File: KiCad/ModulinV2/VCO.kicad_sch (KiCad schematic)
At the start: 99 parts, among them IC13 AS3340D, IC14 AS3340D, IC15 TL074HIDR, IC16 TL074HIDR, IC17 TL072HIDR, Q1 MMBFJ201, Q2 MMBFJ201, SW1 SW_SPDT_MSM

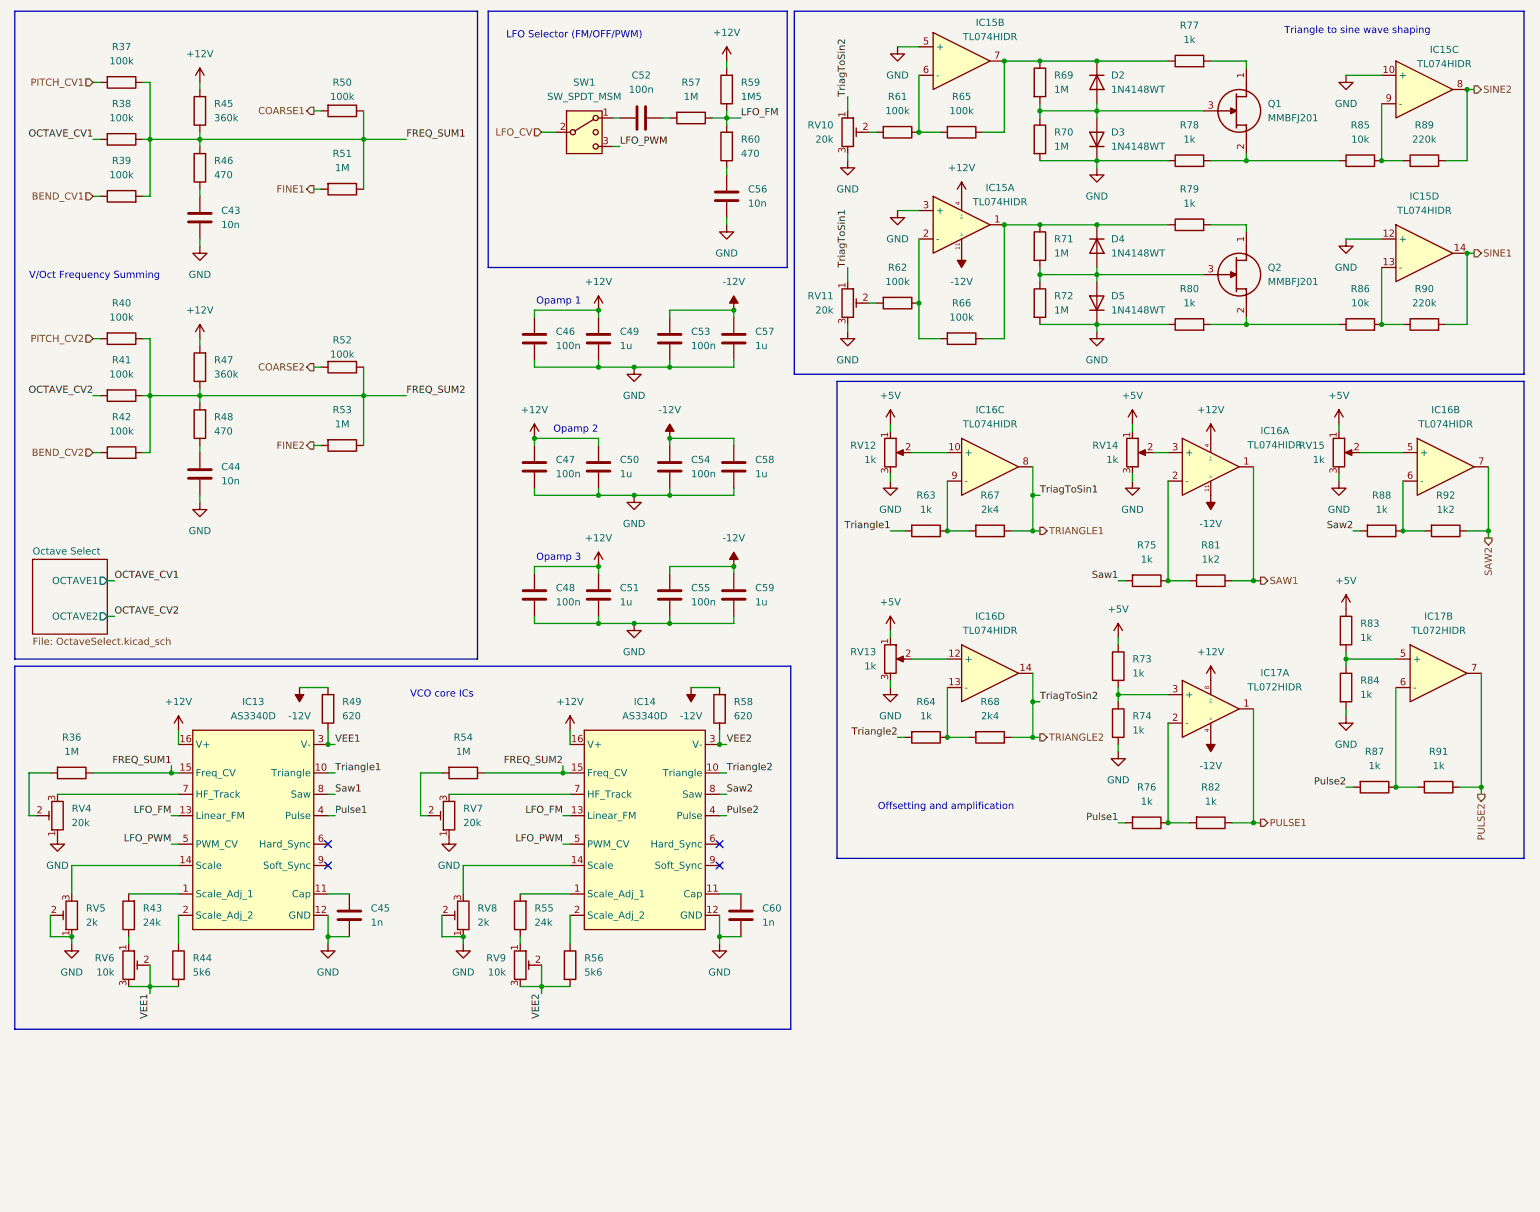
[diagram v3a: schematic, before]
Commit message: Added footprints to all capacitors and potentiometers
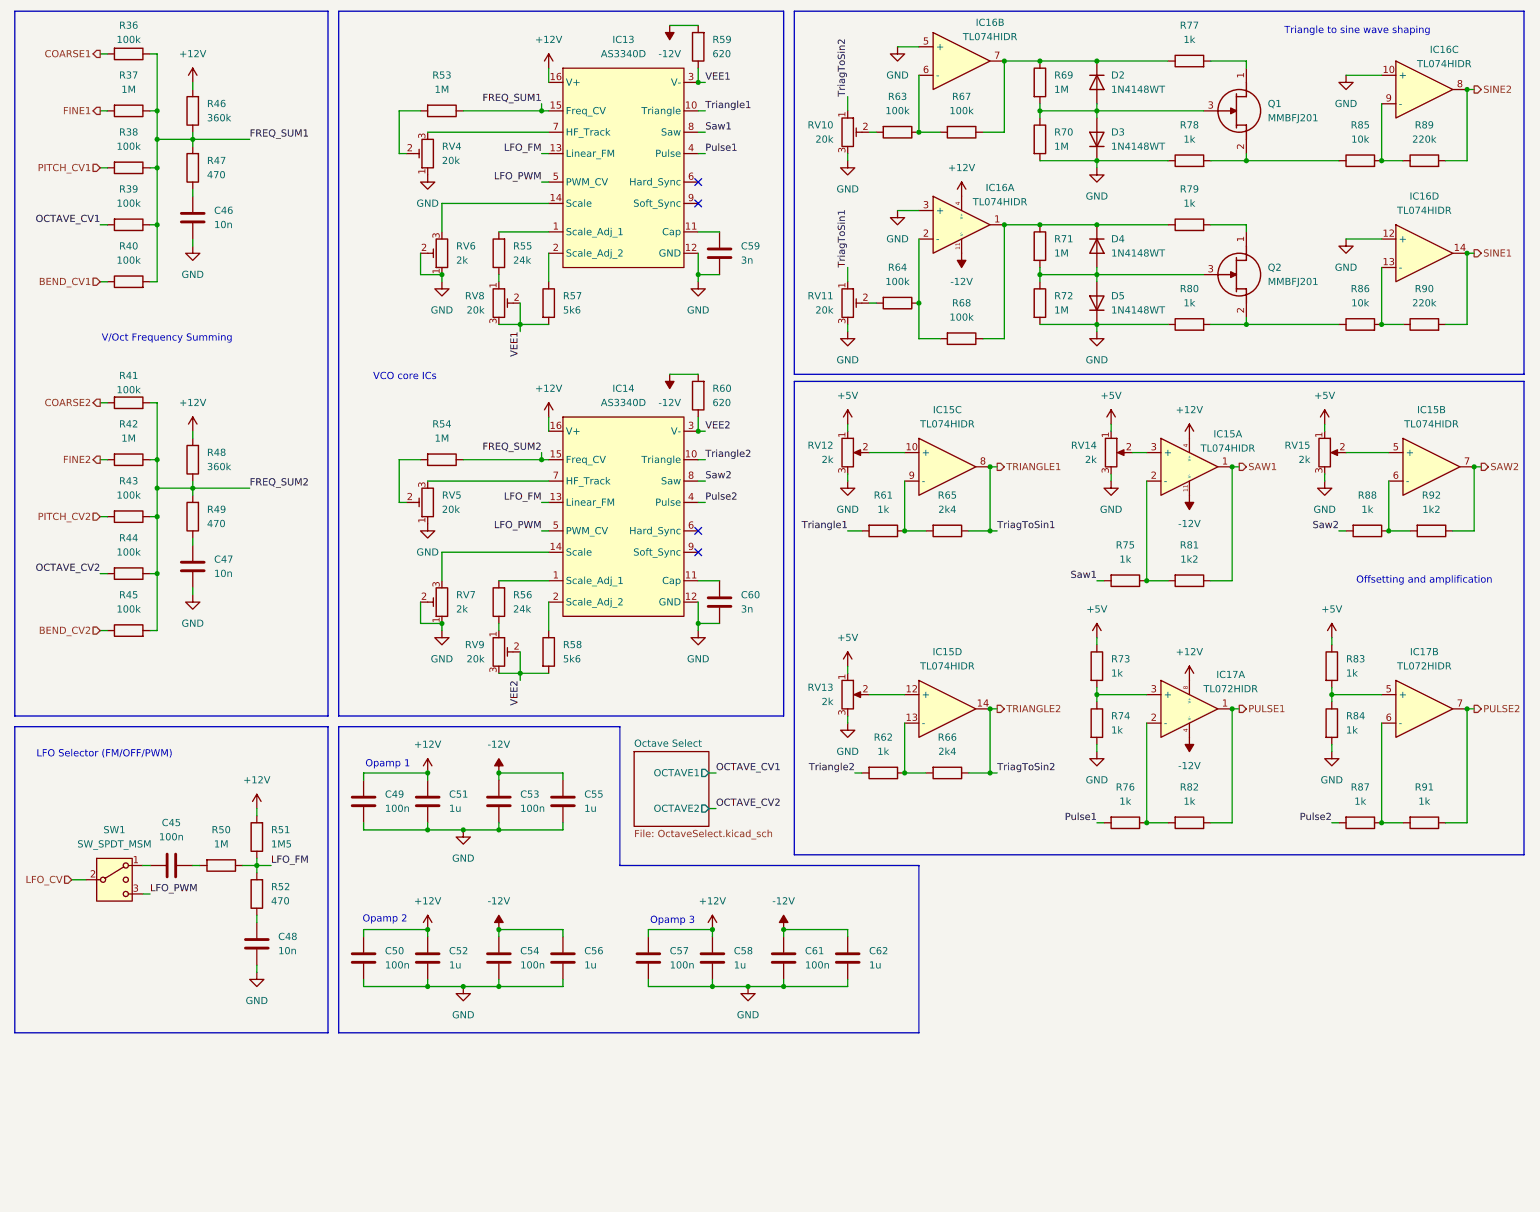
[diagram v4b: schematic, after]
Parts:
- C45: renamed from C52; footprint SamacSys_Parts:CAPC1608X90N -> Capacitor_SMD:C_0603_1608Metric_Pad1.08x0.95mm_HandSolder
- C46: renamed from C43; footprint SamacSys_Parts:CAPC1608X90N -> Capacitor_SMD:C_0603_1608Metric_Pad1.08x0.95mm_HandSolder
- C47: renamed from C44; footprint SamacSys_Parts:CAPC1608X90N -> Capacitor_SMD:C_0603_1608Metric_Pad1.08x0.95mm_HandSolder
- C48: renamed from C56; footprint SamacSys_Parts:CAPC1608X90N -> Capacitor_SMD:C_0603_1608Metric_Pad1.08x0.95mm_HandSolder
- C49: renamed from C46; footprint SamacSys_Parts:CAPC1608X90N -> Capacitor_SMD:C_0603_1608Metric_Pad1.08x0.95mm_HandSolder
- C50: renamed from C47; footprint SamacSys_Parts:CAPC1608X90N -> Capacitor_SMD:C_0603_1608Metric_Pad1.08x0.95mm_HandSolder
- C51: renamed from C49; footprint SamacSys_Parts:CAPC1608X95N -> Capacitor_SMD:C_0603_1608Metric_Pad1.08x0.95mm_HandSolder
- C52: renamed from C50; footprint SamacSys_Parts:CAPC1608X95N -> Capacitor_SMD:C_0603_1608Metric_Pad1.08x0.95mm_HandSolder
- C53, C54: footprint SamacSys_Parts:CAPC1608X90N -> Capacitor_SMD:C_0603_1608Metric_Pad1.08x0.95mm_HandSolder
- C55: renamed from C57; footprint SamacSys_Parts:CAPC1608X95N -> Capacitor_SMD:C_0603_1608Metric_Pad1.08x0.95mm_HandSolder
- C56: renamed from C58; footprint SamacSys_Parts:CAPC1608X95N -> Capacitor_SMD:C_0603_1608Metric_Pad1.08x0.95mm_HandSolder
- C57: renamed from C48; footprint SamacSys_Parts:CAPC1608X90N -> Capacitor_SMD:C_0603_1608Metric_Pad1.08x0.95mm_HandSolder
- C58: renamed from C51; footprint SamacSys_Parts:CAPC1608X95N -> Capacitor_SMD:C_0603_1608Metric_Pad1.08x0.95mm_HandSolder
- C59: renamed from C45; value 1n -> 3n; footprint SamacSys_Parts:CAPC1608X95N -> Capacitor_SMD:C_0603_1608Metric_Pad1.08x0.95mm_HandSolder
- C60: value 1n -> 3n; footprint SamacSys_Parts:CAPC1608X95N -> Capacitor_SMD:C_0603_1608Metric_Pad1.08x0.95mm_HandSolder
- C61: renamed from C55; footprint SamacSys_Parts:CAPC1608X90N -> Capacitor_SMD:C_0603_1608Metric_Pad1.08x0.95mm_HandSolder
- C62: renamed from C59; footprint SamacSys_Parts:CAPC1608X95N -> Capacitor_SMD:C_0603_1608Metric_Pad1.08x0.95mm_HandSolder
- RV10, RV11, RV4: footprint (none) -> SamacSys_Parts:PV36W201C01B00
- RV12, RV13, RV14, RV15: value 1k -> 2k; footprint (none) -> SamacSys_Parts:PV36W201C01B00
- RV5: renamed from RV7; footprint (none) -> SamacSys_Parts:PV36W201C01B00
- RV6: renamed from RV5; footprint (none) -> SamacSys_Parts:PV36W201C01B00
- RV7: renamed from RV8; footprint (none) -> SamacSys_Parts:PV36W201C01B00
- RV8: renamed from RV6; value 10k -> 20k; footprint (none) -> SamacSys_Parts:PV36W201C01B00
- RV9: value 10k -> 20k; footprint (none) -> SamacSys_Parts:PV36W201C01B00
- renumbered IC16 to IC15, IC15 to IC16, R50 to R36, R51 to R37, R37 to R38, R38 to R39, R39 to R40, R52 to R41, R53 to R42, R40 to R43, R41 to R44, R42 to R45, R45 to R46, R46 to R47, R47 to R48, R48 to R49, R57 to R50, R59 to R51, R60 to R52, R36 to R53, R43 to R55, R55 to R56, R44 to R57, R56 to R58, R49 to R59, R58 to R60, R63 to R61, R64 to R62, R61 to R63, R62 to R64, R67 to R65, R68 to R66, R65 to R67, R66 to R68
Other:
- moved on the sheet: C45, C46, C47, C48, C49, C50, C51, C52, C53, C54, C55, C56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

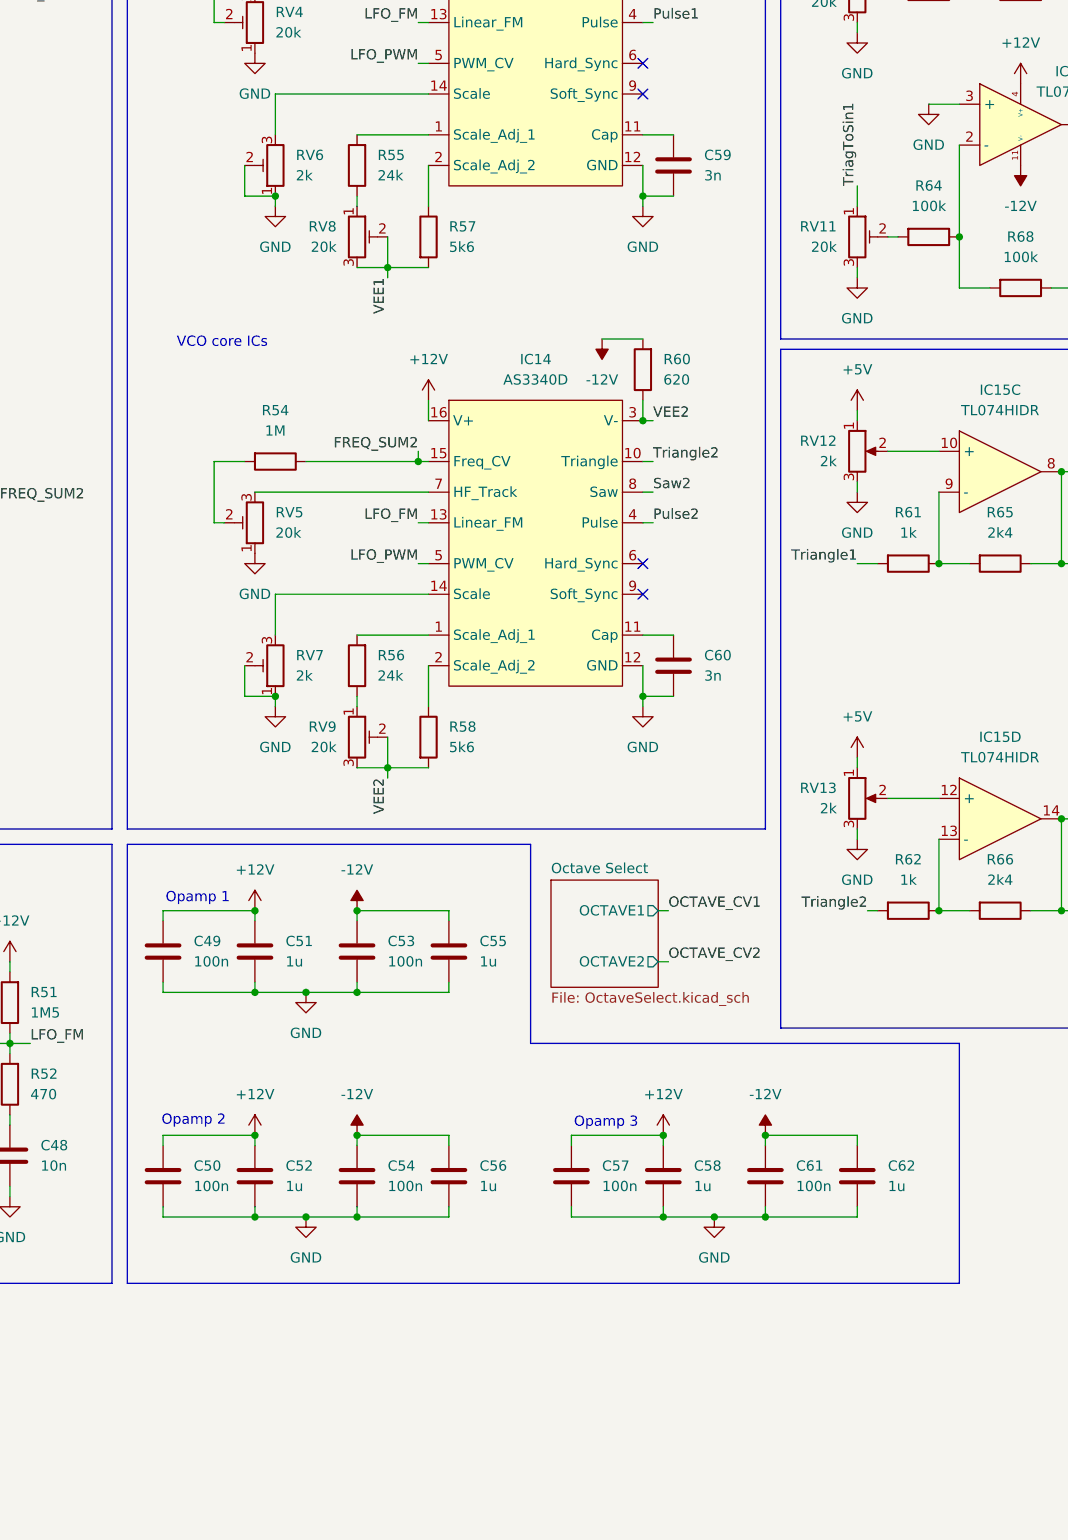
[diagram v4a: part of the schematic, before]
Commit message: Finished Schematic, started on PCB
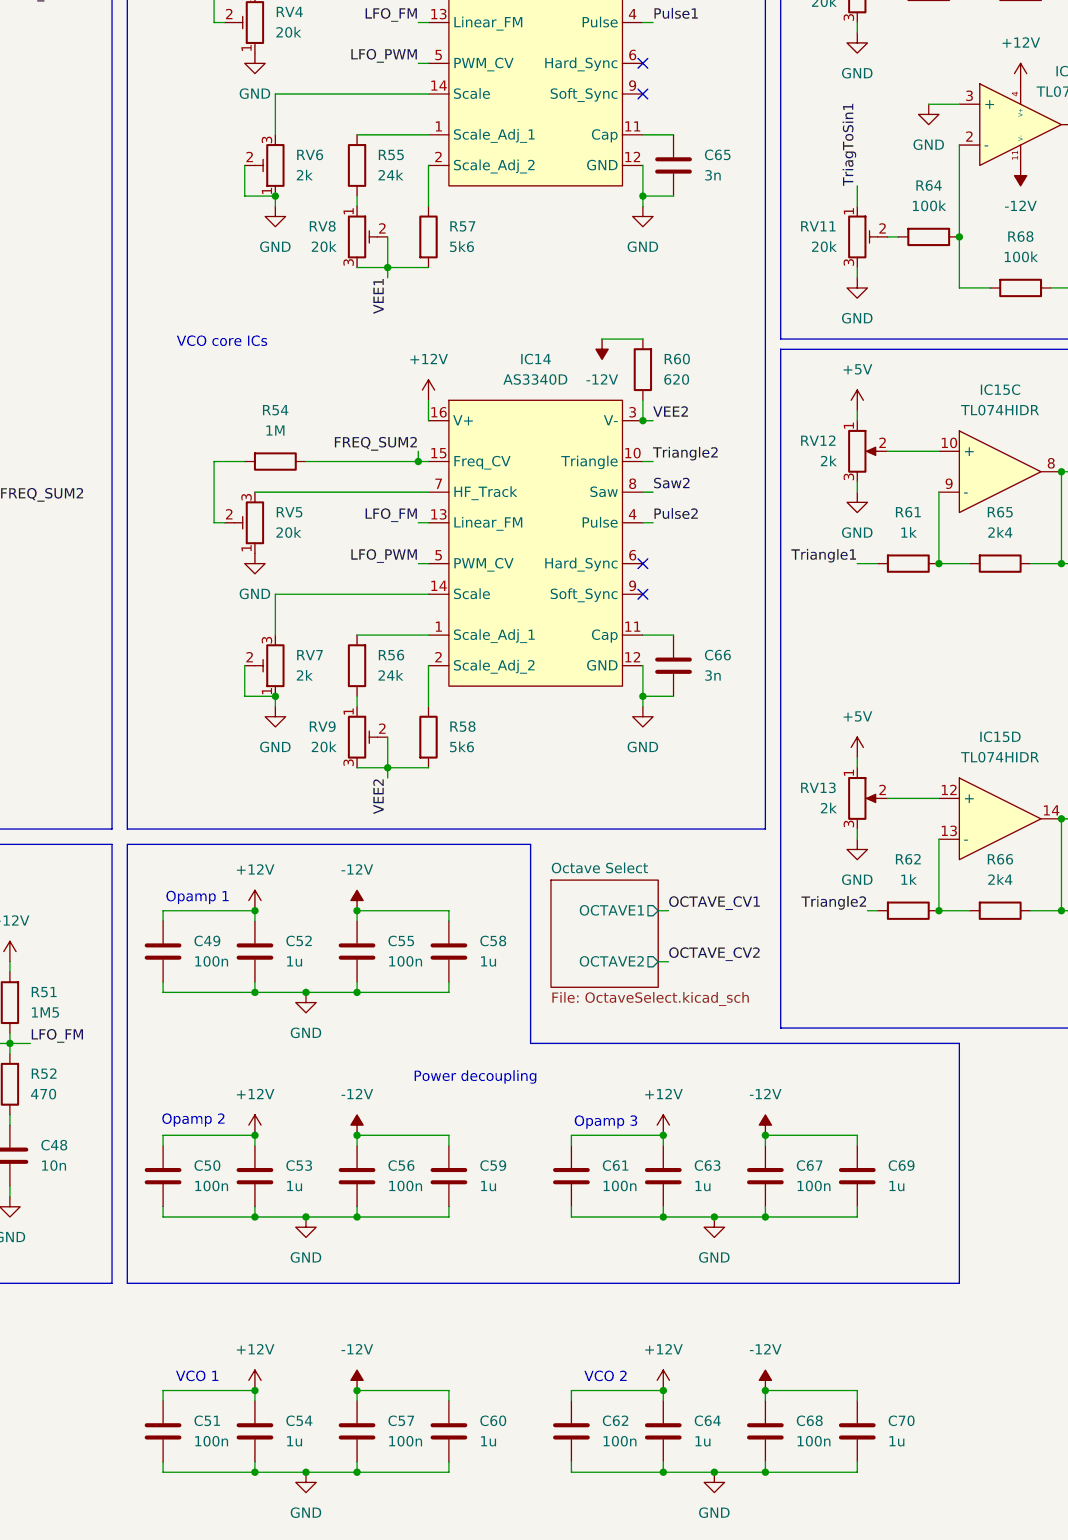
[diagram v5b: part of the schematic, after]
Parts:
- added C51, C57, C62, C68: 100n, Capacitor_SMD:C_0603_1608Metric_Pad1.08x0.95mm_HandSolder, symbol Device:C
- added C54, C60, C64, C70: 1u, Capacitor_SMD:C_0603_1608Metric_Pad1.08x0.95mm_HandSolder, symbol Device:C
- IC13, IC14: footprint SamacSys_Parts:DIP762W46P254L2007H436Q16N -> Package_SO:SOIC-16_3.9x9.9mm_P1.27mm
- R36, R38, R39, R40, R41, R43, R44, R45, R63, R64, R67, R68: footprint (none) -> Resistor_SMD:R_1206_3216Metric_Pad1.30x1.75mm_HandSolder
- R37, R42, R46, R47, R48, R49, R50, R51, R52, R53, R54, R55, R56, R59, R60, R61, R62, R65, R66, R69, R70, R71, R72, R73, R74, R75, R76, R77, R78, R79, R80, R82, R83, R84, R85, R86, R87, R88, R91: footprint (none) -> Resistor_SMD:R_0603_1608Metric_Pad0.98x0.95mm_HandSolder
- R57, R58, R81, R89, R90, R92: footprint (none) -> Resistor_SMD:R_0805_2012Metric_Pad1.20x1.40mm_HandSolder
- renumbered C51 to C52, C52 to C53, C53 to C55, C54 to C56, C55 to C58, C56 to C59, C57 to C61, C58 to C63, C59 to C65, C60 to C66, C61 to C67, C62 to C69
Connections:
- net +12V: now also C51.2, C54.2, C62.2, C64.2
- net -12V: now also C57.2, C60.2, C68.2, C70.2
- net GND: now also C51.1, C54.1, C57.1, C60.1, C62.1, C64.1, C68.1, C70.1
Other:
- note added: "Power decoupling"
- note added: "VCO 1"
- note added: "VCO 2"
